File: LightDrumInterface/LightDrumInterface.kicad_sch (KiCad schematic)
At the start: 72 parts, among them J1 MIDI-IN, J2 0525593652, J3 DEBUG-CONN, J4 PWR-CONN, J5 MIDI-OUT, J6 0541323662, Q1 NX6008NBKWX, Q2 NX6008NBKWX, Q3 NX6008NBKWX, Q4 NX6008NBKWX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

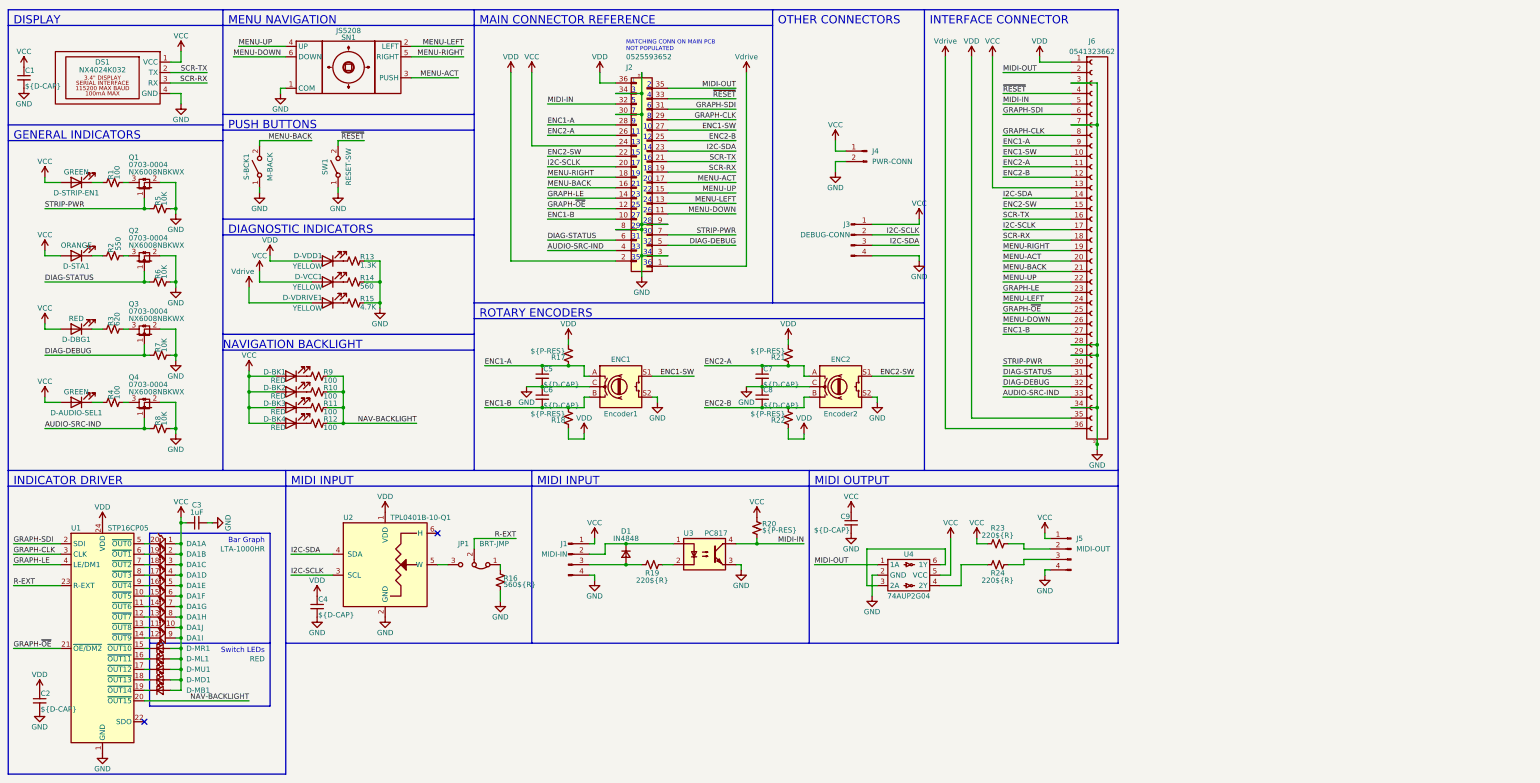
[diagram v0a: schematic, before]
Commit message: Preliminary schematic lock - Starting PCB layout
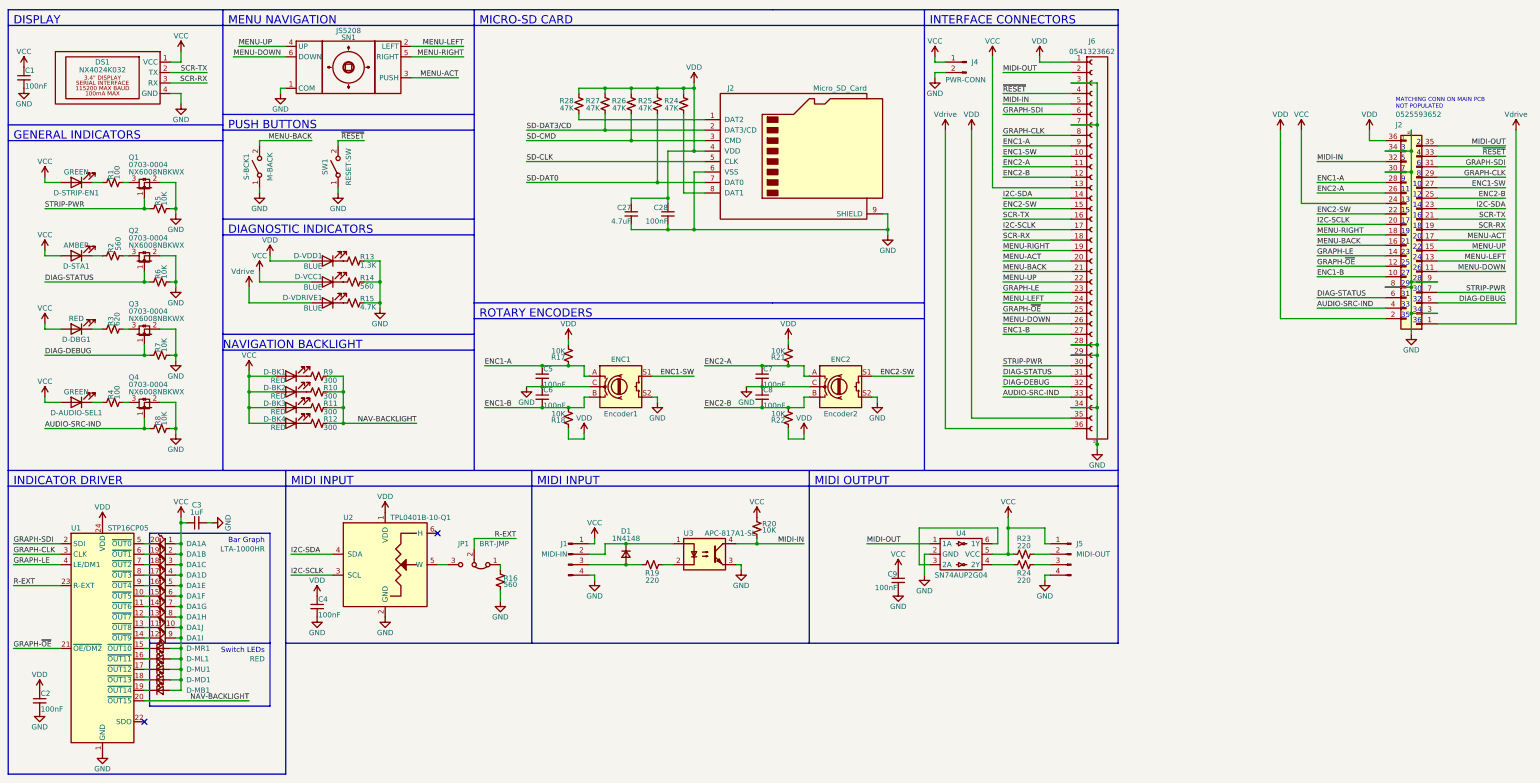
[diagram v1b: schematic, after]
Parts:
- removed J3: DEBUG-CONN, Connector_JST:JST_XH_B4B-XH-A_1x04_P2.50mm_Vertical, symbol Connector:Conn_01x04_Male
- added C27: 4.7uF, Capacitor_SMD:C_0805_2012Metric, symbol Device:C_Small
- added C28: 100nF, Capacitor_SMD:C_0402_1005Metric, symbol Device:C_Small
- added J2: Micro_SD_Card, Daxxn_Connectors:MEM2061-01-188-00-A, symbol Connector:Micro_SD_Card
- added R24, R25, R26, R27, R28: 47K, Resistor_SMD:R_0402_1005Metric, symbol Device:R_Small_US
- C1, C2, C4, C9: value ${D-CAP} -> 100nF; footprint Capacitor_SMD:C_0603_1608Metric -> Capacitor_SMD:C_0402_1005Metric; SupplierPN (none) -> 1276-1043-1-ND
- C3: SupplierPN (none) -> 1276-1102-1-ND
- C5, C6, C7, C8: value ${D-CAP} -> 100nF; footprint Capacitor_SMD:C_0805_2012Metric -> Capacitor_SMD:C_0402_1005Metric; SupplierPN (none) -> 1276-1043-1-ND
- D-AUDIO-SEL1, D-STRIP-EN1: SupplierPN (none) -> 160-1423-1-ND
- D-BK1, D-BK2, D-BK3, D-BK4, D-DBG1, D-MB1, D-MD1, D-ML1, D-MR1, D-MU1: SupplierPN (none) -> 1497-1208-1-ND
- D-STA1: value ORANGE -> AMBER; SupplierPN (none) -> 1830-1081-1-ND
- D-VCC1, D-VDD1, D-VDRIVE1: value YELLOW -> BLUE; SupplierPN (none) -> 1497-1118-1-ND
- D1: value IN4848 -> 1N4148; SupplierPN (none) -> 1N4148WS-FDICT-ND
- DA1: SupplierPN (none) -> 160-1066-ND
- ENC1, ENC2: SupplierPN (none) -> PEC11R-4215F-S0024-ND
- J4: SupplierPN (none) -> 455-2247-ND
- J6: SupplierPN (none) -> WM6784CT-ND
- Q1, Q2, Q3, Q4: SupplierPN (none) -> 1727-NX6008NBKWXCT-ND
- R1, R4: footprint Resistor_SMD:R_0805_2012Metric -> Resistor_SMD:R_0402_1005Metric; SupplierPN (none) -> RMCF0402FT100RCT-ND
- R10, R11, R12, R9: value 100 -> 300; footprint Resistor_SMD:R_0805_2012Metric -> Resistor_SMD:R_0402_1005Metric; SupplierPN (none) -> 311-300LRCT-ND
- R13: footprint Resistor_SMD:R_0805_2012Metric -> Resistor_SMD:R_0402_1005Metric; SupplierPN (none) -> YAG3036CT-ND
- R14: footprint Resistor_SMD:R_0805_2012Metric -> Resistor_SMD:R_0402_1005Metric; SupplierPN (none) -> 13-RC0402FR-13560RLCT-ND
- R15: footprint Resistor_SMD:R_0805_2012Metric -> Resistor_SMD:R_0402_1005Metric; SupplierPN (none) -> RMCF0402FT4K70CT-ND
- R16: value 560${R} -> 560; footprint Resistor_SMD:R_0805_2012Metric -> Resistor_SMD:R_0402_1005Metric; SupplierPN (none) -> 13-RC0402FR-13560RLCT-ND
- R17, R18, R20, R21, R22: value ${P-RES} -> 10K; footprint Resistor_SMD:R_0805_2012Metric -> Resistor_SMD:R_0402_1005Metric; SupplierPN (none) -> 311-10KJRCT-ND
- R19, R23, R24: value 220${R} -> 220; footprint Resistor_SMD:R_0805_2012Metric -> Resistor_SMD:R_0402_1005Metric; SupplierPN (none) -> 1292-WR04X221JTLCT-ND
- R2: value 550 -> 560; footprint Resistor_SMD:R_0805_2012Metric -> Resistor_SMD:R_0402_1005Metric; SupplierPN (none) -> 13-RC0402FR-13560RLCT-ND
- R3: footprint Resistor_SMD:R_0805_2012Metric -> Resistor_SMD:R_0402_1005Metric; SupplierPN (none) -> 311-620LRCT-ND
- R5, R6, R7, R8: footprint Resistor_SMD:R_0805_2012Metric -> Resistor_SMD:R_0402_1005Metric; SupplierPN (none) -> 311-10KJRCT-ND
- S-BCK1, SW1: SupplierPN (none) -> EG5384CT-ND
- SN1: SupplierPN (none) -> EG4561-ND
- U1: SupplierPN (none) -> 497-5743-1-ND
- U2: SupplierPN (none) -> 296-29677-1-ND
- U3: value PC817 -> APC-817A1-SL; footprint Package_DIP:DIP-4_W7.62mm -> Package_DIP:SMDIP-4_W7.62mm; SupplierPN (none) -> 2007-APC-817A1-SLCT-ND
- U4: value 74AUP2G04 -> SN74AUP2G04; SupplierPN (none) -> 296-27353-1-ND
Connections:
- net GND: now also C27.2, C28.2, J2.6 (VSS), J2.9 (SHIELD)
- net VDD: now also C27.1, C28.1, J2.4 (VDD), R24.1, R25.1, R26.1, R27.1, R28.1
- new net: J2.1 (DAT2), R28.2
- new net: J2.8 (DAT1), R24.2
- new net SD-CLK: J2.5 (CLK)
- new net SD-CMD: J2.3 (CMD), R26.2
- new net SD-DAT0: J2.7 (DAT0), R25.2
- new net SD-DAT3/CD: J2.2 (DAT3/CD), R27.2
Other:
- note added: "INTERFACE CONNECTORS"
- note added: "MICRO-SD CARD"
- note removed: "INTERFACE CONNECTOR"
- note removed: "MAIN CONNECTOR REFERENCE"
- note removed: "OTHER CONNECTORS"
- moved on the sheet: C9, J2, J4, J5, R23, R24, U4

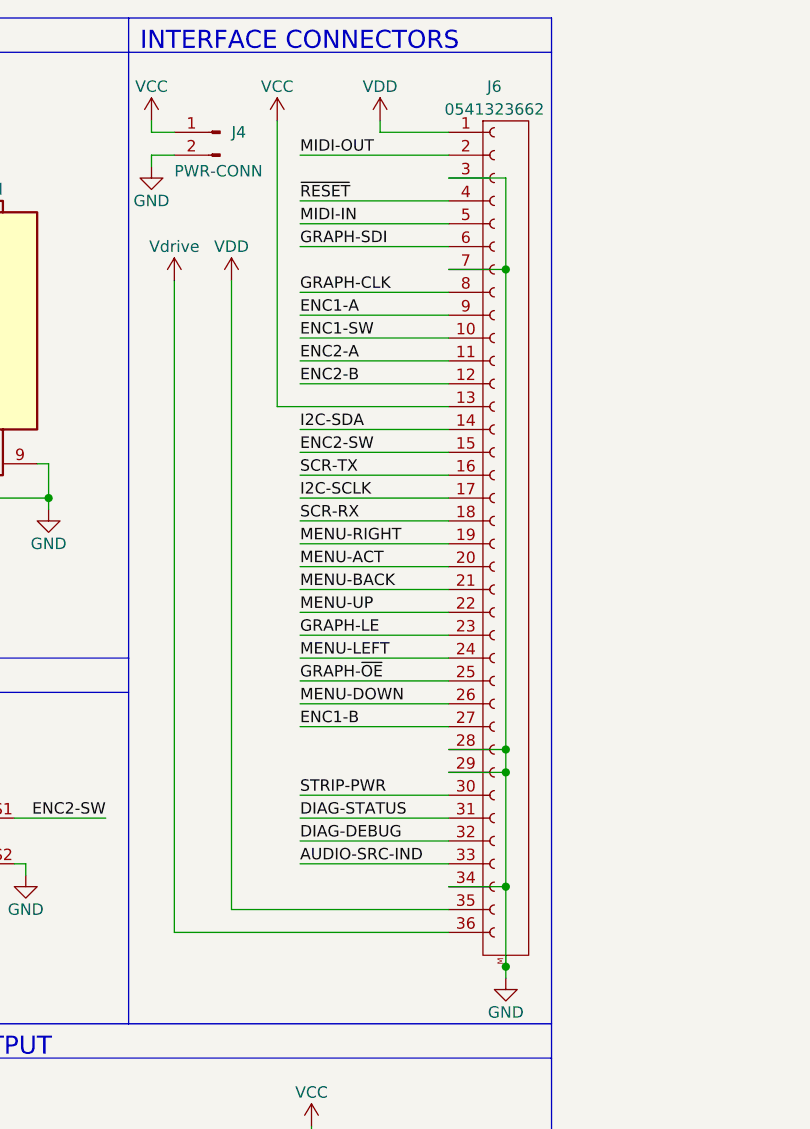
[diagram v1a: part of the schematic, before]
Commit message: Component placement complete
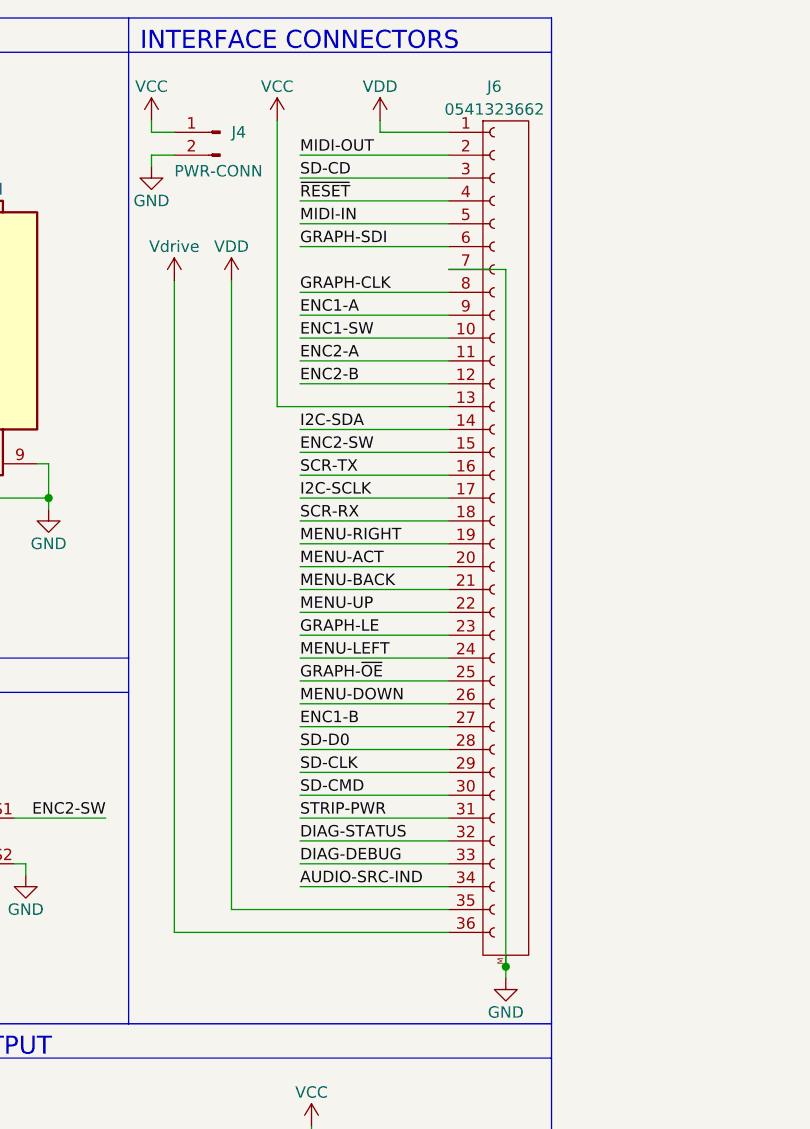
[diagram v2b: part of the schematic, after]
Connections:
- net AUDIO-SRC-IND: now also J6.34 (Pin_34); no longer J6.33 (Pin_33)
- net DIAG-DEBUG: now also J6.33 (Pin_33); no longer J6.32 (Pin_32)
- net DIAG-STATUS: now also J6.32 (Pin_32); no longer J6.31 (Pin_31)
- net GND: no longer J6.28 (Pin_28), J6.29 (Pin_29), J6.3 (Pin_3), J6.34 (Pin_34)
- net SD-CLK: now also J6.29 (Pin_29)
- net SD-CMD: now also J6.30 (Pin_30)
- net STRIP-PWR: now also J6.31 (Pin_31); no longer J6.30 (Pin_30)
- new net SD-CD: J6.3 (Pin_3)
- new net SD-D0: J6.28 (Pin_28)
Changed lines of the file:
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@@
   (junction (at 72.39 101.6) (diameter 0) (color 0 0 0 0)
   )
-  (junction (at 278.13 96.52) (diameter 0) (color 0 0 0 0)
-  )
   (junction (at 143.51 104.14) (diameter 0) (color 0 0 0 0)
   )
@@
   (junction (at 72.39 105.41) (diameter 0) (color 0 0 0 0)
   )
-  (junction (at 278.13 93.98) (diameter 0) (color 0 0 0 0)
-  )
   (junction (at 180.34 31.75) (diameter 0) (color 0 0 0 0)
   )
@@
   (junction (at 354.33 52.07) (diameter 0) (color 0 0 0 0)
   )
-  (junction (at 278.13 109.22) (diameter 0) (color 0 0 0 0)
-  )
   (junction (at 104.14 78.74) (diameter 0) (color 0 0 0 0)
   )
@@
   )
   (junction (at 46.99 114.3) (diameter 0) (color 0 0 0 0)
-  )
-  (junction (at 278.13 40.64) (diameter 0) (color 0 0 0 0)
   )
   (junction (at 149.86 99.06) (diameter 0) (color 0 0 0 0)
@@
     (stroke (width 0) (type default))
   )
-  (wire (pts (xy 255.27 101.6) (xy 271.78 101.6))
+  (wire (pts (xy 255.27 104.14) (xy 271.78 104.14))
     (stroke (width 0) (type default))
   )
@@
     (stroke (width 0) (type default))
   )
+  (wire (pts (xy 255.27 93.98) (xy 271.78 93.98))
+    (stroke (width 0) (type default))
+  )
   (wire (pts (xy 111.76 21.59) (xy 124.46 21.59))
     (stroke (width 0) (type default))
@@
     (stroke (width 0) (type default))
   )
+  (wire (pts (xy 255.27 96.52) (xy 271.78 96.52))
+    (stroke (width 0) (type default))
+  )
   (wire (pts (xy 139.7 44.45) (xy 165.1 44.45))
     (stroke (width 0) (type default))
   )
-  (wire (pts (xy 278.13 93.98) (xy 278.13 96.52))
+  (wire (pts (xy 278.13 40.64) (xy 278.13 118.11))
     (stroke (width 0) (type default))
   )
@@
     (stroke (width 0) (type default))
   )
-  (wire (pts (xy 278.13 30.48) (xy 278.13 40.64))
-    (stroke (width 0) (type default))
-  )
   (wire (pts (xy 173.99 66.04) (xy 180.34 66.04))
     (stroke (width 0) (type default))
@@
     (stroke (width 0) (type default))
   )
-  (wire (pts (xy 255.27 106.68) (xy 271.78 106.68))
+  (wire (pts (xy 255.27 109.22) (xy 271.78 109.22))
     (stroke (width 0) (type default))
   )
@@
     (stroke (width 0) (type default))
   )
-  (wire (pts (xy 278.13 96.52) (xy 278.13 109.22))
-    (stroke (width 0) (type default))
-  )
   (wire (pts (xy 271.78 63.5) (xy 255.27 63.5))
     (stroke (width 0) (type default))
@@
     (stroke (width 0) (type default))
   )
-  (wire (pts (xy 271.78 104.14) (xy 255.27 104.14))
+  (wire (pts (xy 271.78 106.68) (xy 255.27 106.68))
     (stroke (width 0) (type default))
   )
@@
     (stroke (width 0) (type default))
   )
+  (wire (pts (xy 255.27 99.06) (xy 271.78 99.06))
+    (stroke (width 0) (type default))
+  )
   (wire (pts (xy 207.01 106.68) (xy 207.01 109.22))
     (stroke (width 0) (type default))
@@
     (stroke (width 0) (type default))
   )
-  (wire (pts (xy 271.78 30.48) (xy 278.13 30.48))
-    (stroke (width 0) (type default))
-  )
   (wire (pts (xy 54.61 60.96) (xy 54.61 62.23))
     (stroke (width 0) (type default))
@@
     (stroke (width 0) (type default))
   )
+  (wire (pts (xy 255.27 30.48) (xy 271.78 30.48))
+    (stroke (width 0) (type default))
+  )
   (wire (pts (xy 54.61 144.78) (xy 55.88 144.78))
     (stroke (width 0) (type default))
@@
   )
   (wire (pts (xy 255.27 76.2) (xy 271.78 76.2))
-    (stroke (width 0) (type default))
-  )
-  (wire (pts (xy 278.13 109.22) (xy 278.13 118.11))
     (stroke (width 0) (type default))
   )
@@
     (stroke (width 0) (type default))
   )
-  (wire (pts (xy 271.78 99.06) (xy 255.27 99.06))
+  (wire (pts (xy 271.78 101.6) (xy 255.27 101.6))
     (stroke (width 0) (type default))
   )
@@
     (stroke (width 0) (type default))
   )
-  (wire (pts (xy 271.78 96.52) (xy 278.13 96.52))
-    (stroke (width 0) (type default))
-  )
   (wire (pts (xy 139.7 41.91) (xy 158.75 41.91))
     (stroke (width 0) (type default))
@@
     (stroke (width 0) (type default))
   )
-  (wire (pts (xy 271.78 93.98) (xy 278.13 93.98))
-    (stroke (width 0) (type default))
-  )
   (wire (pts (xy 195.58 142.24) (xy 195.58 140.97))
     (stroke (width 0) (type default))
@@
     (stroke (width 0) (type default))
   )
-  (wire (pts (xy 271.78 109.22) (xy 278.13 109.22))
-    (stroke (width 0) (type default))
-  )
   (wire (pts (xy 278.13 119.38) (xy 278.13 118.11))
     (stroke (width 0) (type default))
@@
   )
   (wire (pts (xy 173.99 66.04) (xy 165.1 66.04))
-    (stroke (width 0) (type default))
-  )
-  (wire (pts (xy 278.13 40.64) (xy 278.13 93.98))
     (stroke (width 0) (type default))
   )
@@
     (effects (font (size 1.27 1.27)) (justify left bottom))
   )
-  (label "DIAG-DEBUG" (at 255.27 104.14 0) (fields_autoplaced)
+  (label "DIAG-DEBUG" (at 255.27 106.68 0) (fields_autoplaced)
     (effects (font (size 1.27 1.27)) (justify left bottom))
   )
@@
     (effects (font (size 1.27 1.27)) (justify left bottom))
   )
-  (label "AUDIO-SRC-IND" (at 255.27 106.68 0) (fields_autoplaced)
+  (label "AUDIO-SRC-IND" (at 255.27 109.22 0) (fields_autoplaced)
+    (effects (font (size 1.27 1.27)) (justify left bottom))
+  )
+  (label "SD-CLK" (at 255.27 96.52 0) (fields_autoplaced)
     (effects (font (size 1.27 1.27)) (justify left bottom))
   )
@@
     (effects (font (size 1.27 1.27)) (justify right bottom))
   )
-  (label "STRIP-PWR" (at 255.27 99.06 0) (fields_autoplaced)
+  (label "STRIP-PWR" (at 255.27 101.6 0) (fields_autoplaced)
     (effects (font (size 1.27 1.27)) (justify left bottom))
   )
@@
     (effects (font (size 1.27 1.27)) (justify left bottom))
   )
+  (label "SD-D0" (at 255.27 93.98 0) (fields_autoplaced)
+    (effects (font (size 1.27 1.27)) (justify left bottom))
+  )
+  (label "SD-CMD" (at 255.27 99.06 0) (fields_autoplaced)
+    (effects (font (size 1.27 1.27)) (justify left bottom))
+  )
   (label "MENU-ACT" (at 255.27 73.66 0) (fields_autoplaced)
     (effects (font (size 1.27 1.27)) (justify left bottom))
   )
-  (label "DIAG-STATUS" (at 255.27 101.6 0) (fields_autoplaced)
+  (label "DIAG-STATUS" (at 255.27 104.14 0) (fields_autoplaced)
     (effects (font (size 1.27 1.27)) (justify left bottom))
   )
@@
     (effects (font (size 1.27 1.27)) (justify left bottom))
   )
+  (label "SD-CD" (at 255.27 30.48 0) (fields_autoplaced)
+    (effects (font (size 1.27 1.27)) (justify left bottom))
+  )
